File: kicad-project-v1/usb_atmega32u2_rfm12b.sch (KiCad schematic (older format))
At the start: 19 parts, among them K1 CONN_3, P1 CONN_7, P2 CONN_1, P3 CONN_4, P4 CONN_6, SW1 HWB, SW2 RESET, U1 ATMEGA32U2, U2 RFM12, U3 USBCONN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

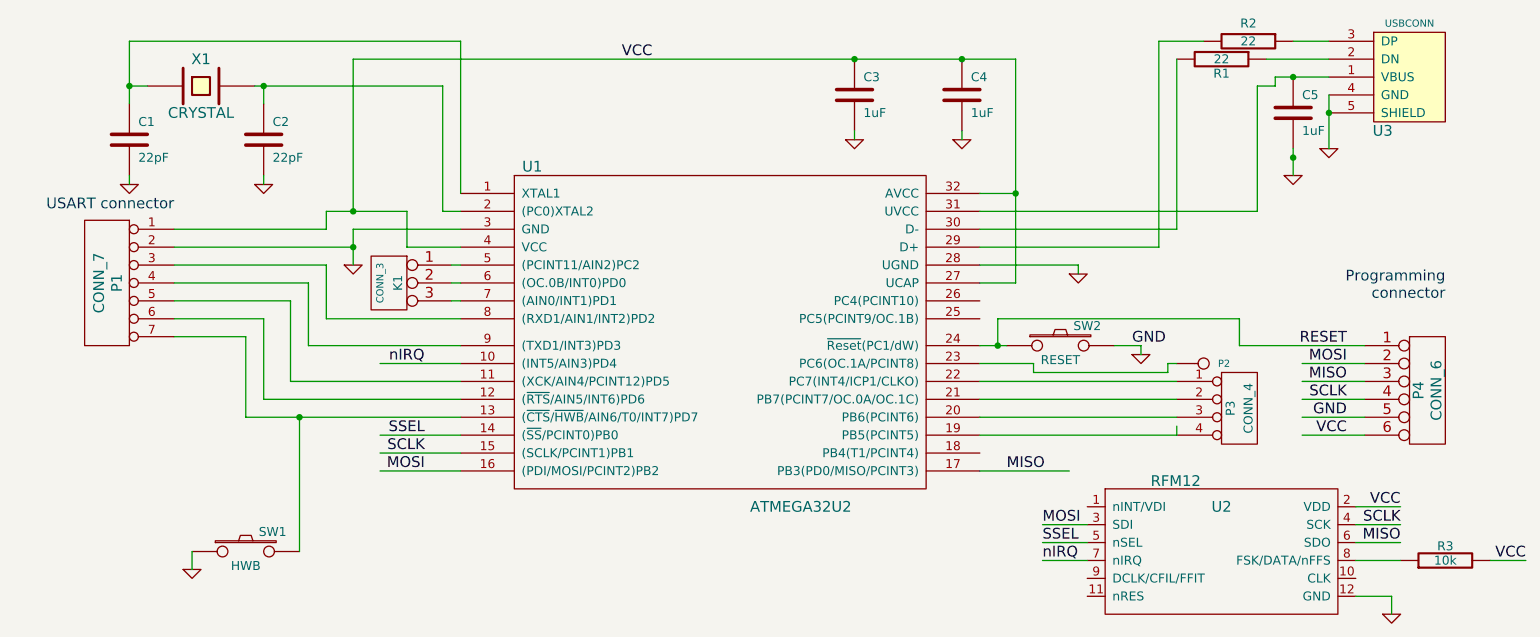
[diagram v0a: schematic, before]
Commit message: Added pull-up resistors on HWB and RESET.
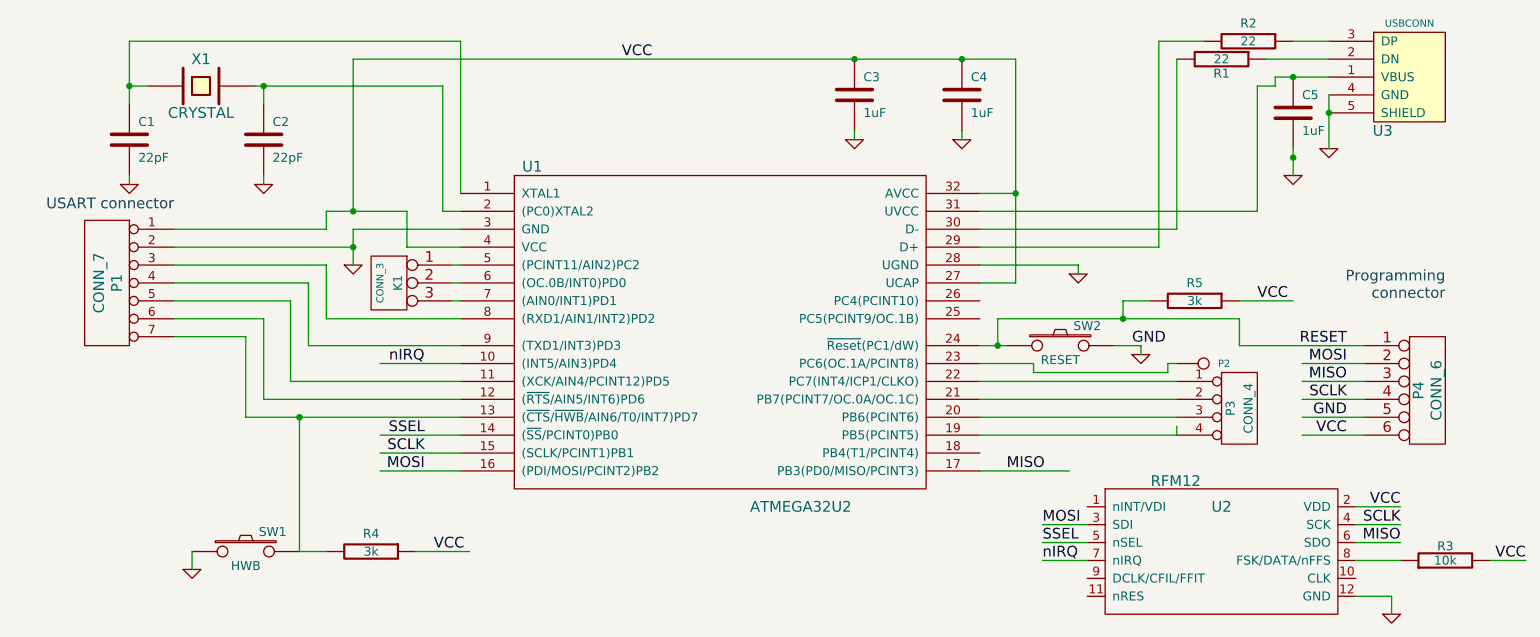
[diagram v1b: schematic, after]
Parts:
- added R4, R5: 3k, symbol R
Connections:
- wire segments 98 -> 103
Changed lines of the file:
@@
 Sheet 1 1
 Title ""
-Date "3 nov 2013"
+Date "6 dec 2013"
 Rev ""
 Comp ""
@@
 	4100 4100 3650 4100
 $Comp
-L GND #PWR01
+L GND #PWR11
 U 1 1 525ED47E
 P 9300 5500
-F 0 "#PWR01" H 9300 5500 30  0001 C CNN
+F 0 "#PWR11" H 9300 5500 30  0001 C CNN
 F 1 "GND" H 9300 5430 30  0001 C CNN
 F 2 "" H 9300 5500 60  0001 C CNN
@@
 VCC
 $Comp
-L GND #PWR02
+L GND #PWR4
 U 1 1 52596CFE
 P 3500 3550
-F 0 "#PWR02" H 3500 3550 30  0001 C CNN
+F 0 "#PWR4" H 3500 3550 30  0001 C CNN
 F 1 "GND" H 3500 3480 30  0001 C CNN
 F 2 "" H 3500 3550 60  0001 C CNN
@@
 $EndComp
 $Comp
-L GND #PWR03
+L GND #PWR5
 U 1 1 52595544
 P 6300 2850
-F 0 "#PWR03" H 6300 2850 30  0001 C CNN
+F 0 "#PWR5" H 6300 2850 30  0001 C CNN
 F 1 "GND" H 6300 2780 30  0001 C CNN
 F 2 "" H 6300 2850 60  0001 C CNN
@@
 $EndComp
 $Comp
-L GND #PWR04
+L GND #PWR8
 U 1 1 5259502D
 P 7900 4050
-F 0 "#PWR04" H 7900 4050 30  0001 C CNN
+F 0 "#PWR8" H 7900 4050 30  0001 C CNN
 F 1 "GND" H 7900 3980 30  0001 C CNN
 F 2 "" H 7900 4050 60  0001 C CNN
@@
 $EndComp
 $Comp
-L GND #PWR05
+L GND #PWR2
 U 1 1 52595014
 P 2600 5250
-F 0 "#PWR05" H 2600 5250 30  0001 C CNN
+F 0 "#PWR2" H 2600 5250 30  0001 C CNN
 F 1 "GND" H 2600 5180 30  0001 C CNN
 F 2 "" H 2600 5250 60  0001 C CNN
@@
 $EndComp
 $Comp
-L GND #PWR06
+L GND #PWR7
 U 1 1 4CE7DFC3
 P 7550 3600
-F 0 "#PWR06" H 7550 3600 30  0001 C CNN
+F 0 "#PWR7" H 7550 3600 30  0001 C CNN
 F 1 "GND" H 7550 3530 30  0001 C CNN
 F 2 "" H 7550 3600 60  0001 C CNN
@@
 $EndComp
 $Comp
-L GND #PWR07
+L GND #PWR6
 U 1 1 4CE7DCD9
 P 6900 2850
-F 0 "#PWR07" H 6900 2850 30  0001 C CNN
+F 0 "#PWR6" H 6900 2850 30  0001 C CNN
 F 1 "GND" H 6900 2780 30  0001 C CNN
 F 2 "" H 6900 2850 60  0001 C CNN
@@
 $EndComp
 $Comp
-L GND #PWR08
+L GND #PWR3
 U 1 1 4CD7B9C9
 P 3000 3100
-F 0 "#PWR08" H 3000 3100 30  0001 C CNN
+F 0 "#PWR3" H 3000 3100 30  0001 C CNN
 F 1 "GND" H 3000 3030 30  0001 C CNN
 F 2 "" H 3000 3100 60  0001 C CNN
@@
 $EndComp
 $Comp
-L GND #PWR09
+L GND #PWR1
 U 1 1 4CD7B9C5
 P 2250 3100
-F 0 "#PWR09" H 2250 3100 30  0001 C CNN
+F 0 "#PWR1" H 2250 3100 30  0001 C CNN
 F 1 "GND" H 2250 3030 30  0001 C CNN
 F 2 "" H 2250 3100 60  0001 C CNN
@@
 $EndComp
 $Comp
-L GND #PWR010
+L GND #PWR10
 U 1 1 4CD71B50
 P 8950 2900
-F 0 "#PWR010" H 8950 2900 30  0001 C CNN
+F 0 "#PWR10" H 8950 2900 30  0001 C CNN
 F 1 "GND" H 8950 2830 30  0001 C CNN
 F 2 "" H 8950 2900 60  0001 C CNN
@@
 $EndComp
 $Comp
-L GND #PWR011
+L GND #PWR9
 U 1 1 4CD71B2E
 P 8750 3050
-F 0 "#PWR011" H 8750 3050 30  0001 C CNN
+F 0 "#PWR9" H 8750 3050 30  0001 C CNN
 F 1 "GND" H 8750 2980 30  0001 C CNN
 F 2 "" H 8750 3050 60  0001 C CNN
@@
 	1    0    0    -1
 $EndComp
+$Comp
+L R R4
+U 1 1 52A118DC
+P 3600 5150
+F 0 "R4" V 3500 5150 50  0000 C CNN
+F 1 "3k" V 3600 5150 50  0000 C CNN
+F 2 "" H 3600 5150 60  0001 C CNN
+F 3 "" H 3600 5150 60  0001 C CNN
+	1    3600 5150
+	0    1    1    0
+$EndComp
+Wire Wire Line
+	3850 5150 4150 5150
+Text Label 3950 5150 0    60   ~ 0
+VCC
+Wire Wire Line
+	3350 5150 3200 5150
+$Comp
+L R R5
+U 1 1 52A119C3
+P 8200 3750
+F 0 "R5" V 8100 3750 50  0000 C CNN
+F 1 "3k" V 8200 3750 50  0000 C CNN
+F 2 "" H 8200 3750 60  0001 C CNN
+F 3 "" H 8200 3750 60  0001 C CNN
+	1    8200 3750
+	0    1    1    0
+$EndComp
+Wire Wire Line
+	8450 3750 8750 3750
+Text Label 8550 3750 0    60   ~ 0
+VCC
+Wire Wire Line
+	7950 3750 7800 3750
+Wire Wire Line
+	7800 3750 7800 3850
+Connection ~ 7800 3850
 $EndSCHEMATC
